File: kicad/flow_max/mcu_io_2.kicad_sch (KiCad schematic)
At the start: 1 part, among them U5 MCXN947VDFT

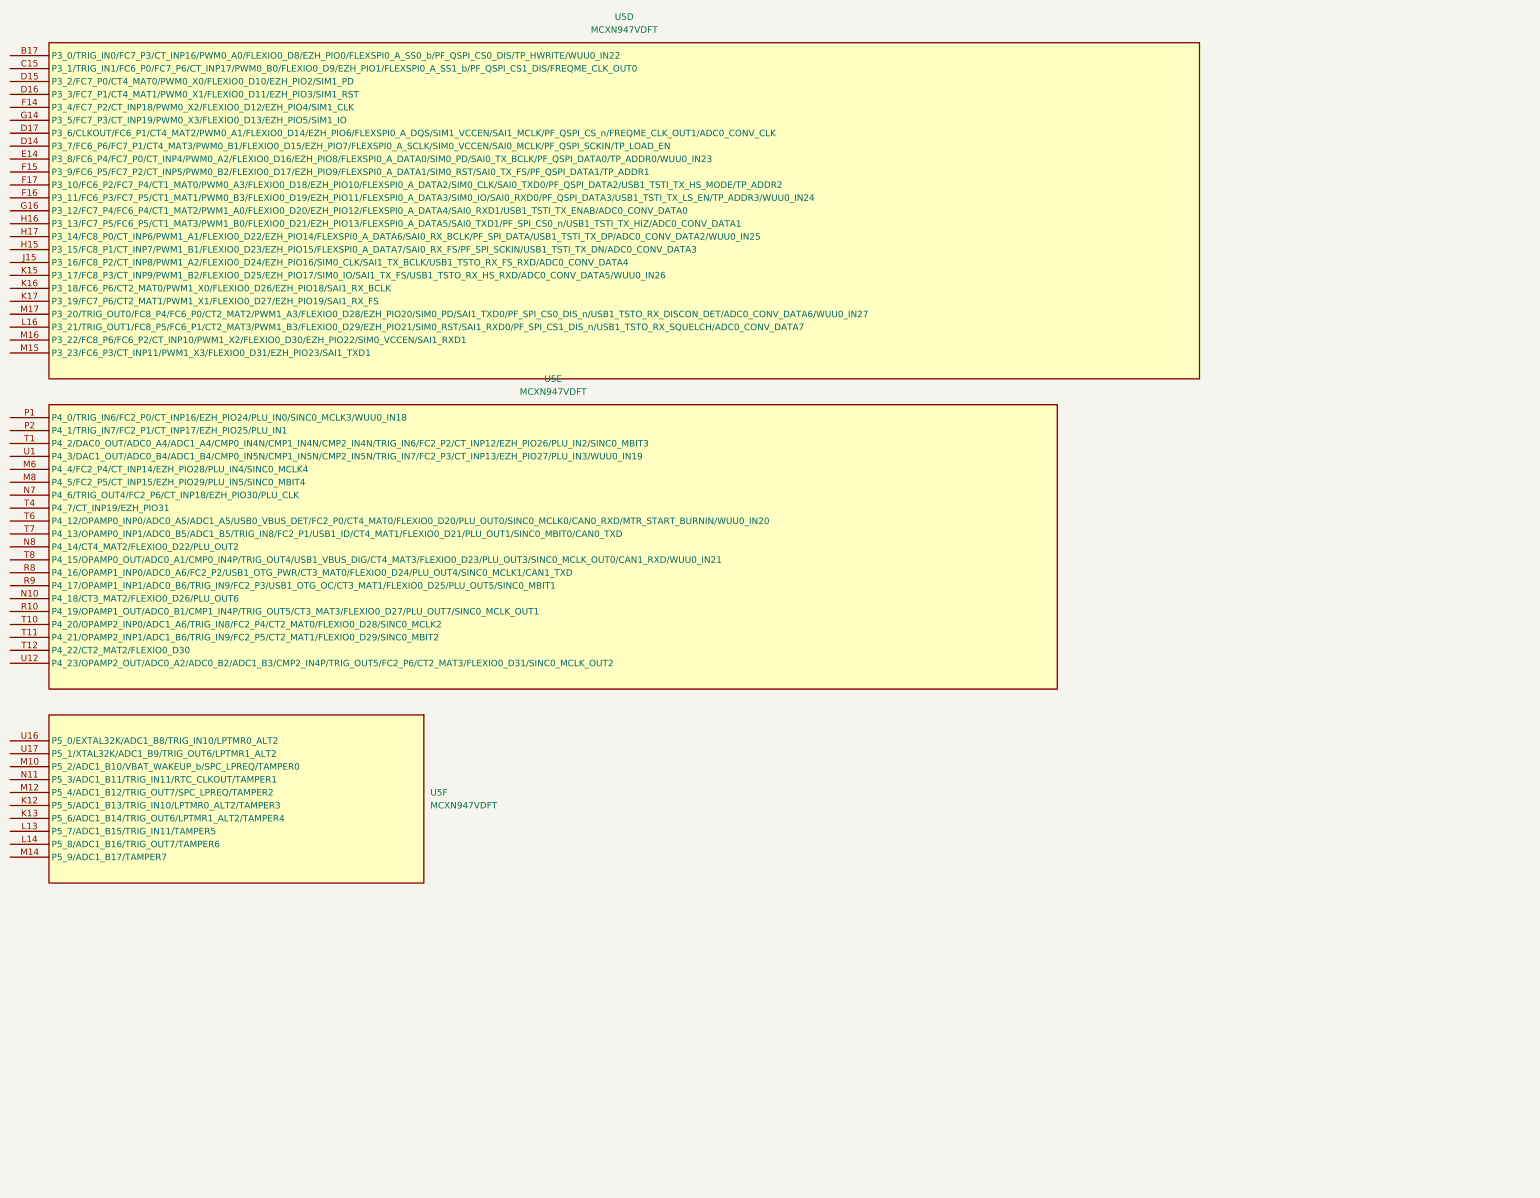
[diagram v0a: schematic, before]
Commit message: Added pin assignment to MCXN947 for the communication lines, Debugger, ISP_Mode and optional GPIO/SD card
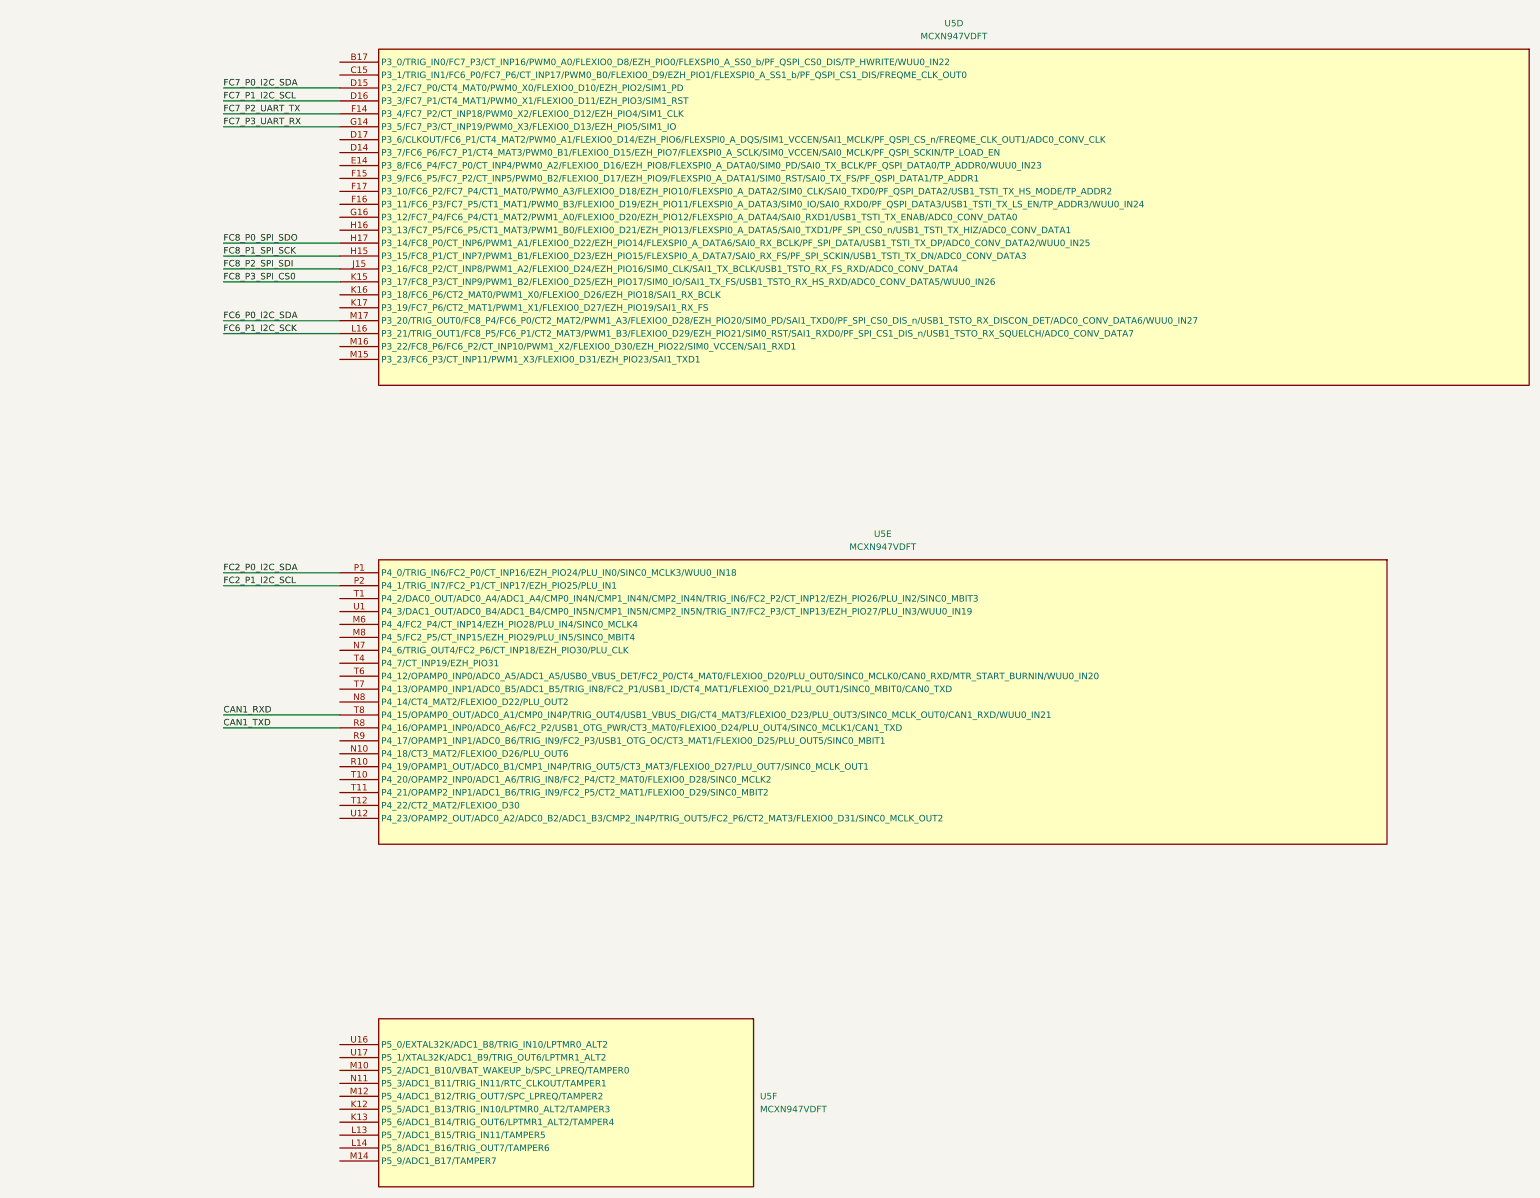
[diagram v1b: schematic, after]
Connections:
- net FC2_P0_I2C_SDA: now reaches U5.P1 (P4_0/TRIG_IN6/FC2_P0/CT_INP16/EZH_PIO24/PLU_IN0/SINC0_MCLK3/WUU0_IN18)
- net FC2_P1_I2C_SCL: now reaches U5.P2 (P4_1/TRIG_IN7/FC2_P1/CT_INP17/EZH_PIO25/PLU_IN1)
- net CAN1_TXD: now reaches U5.R8 (P4_16/OPAMP1_INP0/ADC0_A6/FC2_P2/USB1_OTG_PWR/CT3_MAT0/FLEXIO0_D24/PLU_OUT4/SINC0_MCLK1/CAN1_TXD)
- net CAN1_RXD: now reaches U5.T8 (P4_15/OPAMP0_OUT/ADC0_A1/CMP0_IN4P/TRIG_OUT4/USB1_VBUS_DIG/CT4_MAT3/FLEXIO0_D23/PLU_OUT3/SINC0_MCLK_OUT0/CAN1_RXD/WUU0_IN21)
- net FC7_P0_I2C_SDA: now reaches U5.D15 (P3_2/FC7_P0/CT4_MAT0/PWM0_X0/FLEXIO0_D10/EZH_PIO2/SIM1_PD)
- net FC7_P1_I2C_SCL: now reaches U5.D16 (P3_3/FC7_P1/CT4_MAT1/PWM0_X1/FLEXIO0_D11/EZH_PIO3/SIM1_RST)
- net FC7_P2_UART_TX: now reaches U5.F14 (P3_4/FC7_P2/CT_INP18/PWM0_X2/FLEXIO0_D12/EZH_PIO4/SIM1_CLK)
- net FC7_P3_UART_RX: now reaches U5.G14 (P3_5/FC7_P3/CT_INP19/PWM0_X3/FLEXIO0_D13/EZH_PIO5/SIM1_IO)
- net FC8_P1_SPI_SCK: now reaches U5.H15 (P3_15/FC8_P1/CT_INP7/PWM1_B1/FLEXIO0_D23/EZH_PIO15/FLEXSPI0_A_DATA7/SAI0_RX_FS/PF_SPI_SCKIN/USB1_TSTI_TX_DN/ADC0_CONV_DATA3)
- net FC8_P0_SPI_SDO: now reaches U5.H17 (P3_14/FC8_P0/CT_INP6/PWM1_A1/FLEXIO0_D22/EZH_PIO14/FLEXSPI0_A_DATA6/SAI0_RX_BCLK/PF_SPI_DATA/USB1_TSTI_TX_DP/ADC0_CONV_DATA2/WUU0_IN25)
- net FC8_P2_SPI_SDI: now reaches U5.J15 (P3_16/FC8_P2/CT_INP8/PWM1_A2/FLEXIO0_D24/EZH_PIO16/SIM0_CLK/SAI1_TX_BCLK/USB1_TSTO_RX_FS_RXD/ADC0_CONV_DATA4)
- net FC8_P3_SPI_CS0: now reaches U5.K15 (P3_17/FC8_P3/CT_INP9/PWM1_B2/FLEXIO0_D25/EZH_PIO17/SIM0_IO/SAI1_TX_FS/USB1_TSTO_RX_HS_RXD/ADC0_CONV_DATA5/WUU0_IN26)
- net FC6_P1_I2C_SCK: now reaches U5.L16 (P3_21/TRIG_OUT1/FC8_P5/FC6_P1/CT2_MAT3/PWM1_B3/FLEXIO0_D29/EZH_PIO21/SIM0_RST/SAI1_RXD0/PF_SPI_CS1_DIS_n/USB1_TSTO_RX_SQUELCH/ADC0_CONV_DATA7)
- net FC6_P0_I2C_SDA: now reaches U5.M17 (P3_20/TRIG_OUT0/FC8_P4/FC6_P0/CT2_MAT2/PWM1_A3/FLEXIO0_D28/EZH_PIO20/SIM0_PD/SAI1_TXD0/PF_SPI_CS0_DIS_n/USB1_TSTO_RX_DISCON_DET/ADC0_CONV_DATA6/WUU0_IN27)
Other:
- moved on the sheet: U5D, U5E, U5F
